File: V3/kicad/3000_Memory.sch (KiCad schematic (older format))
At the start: 4 parts, among them U3000 SST39SF040, U3001 AS6C4008-55PCN

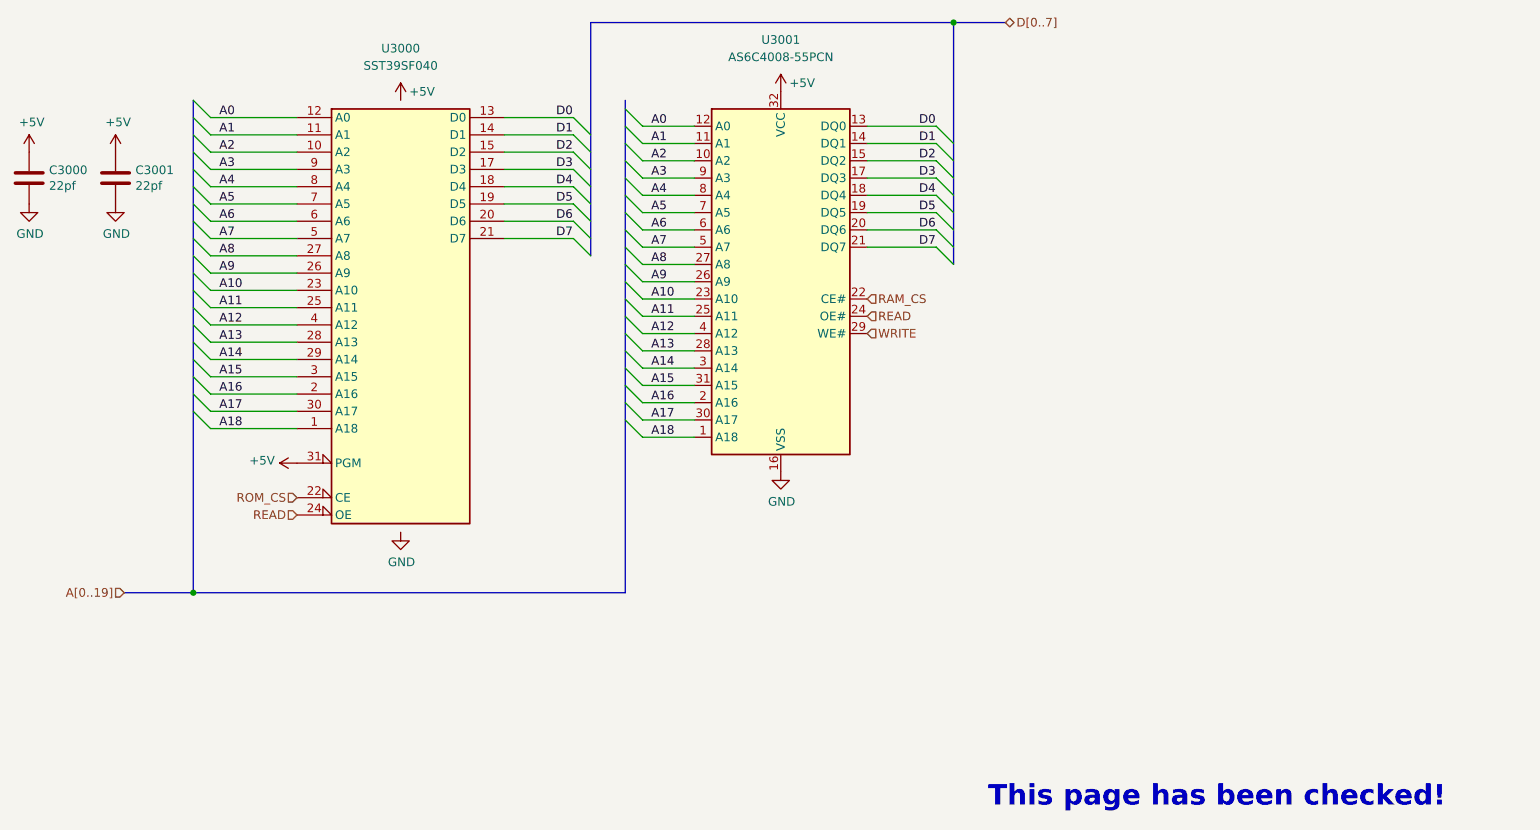
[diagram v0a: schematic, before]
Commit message: 3 1 1 m memory (#15)
* moved EEPROM files to /old

* Reworking 3.0 board

* changed footprint on RAM chip

* cleared out old memory traces

* started on rerouting

* on to autoroute

* little more cleanup

* more cleanup

* ill let the autoroute do the rest

* reroute complete

* made PQFP leads fatter

* Updated GAL logic

* Design Rule Check

* Minor pcb touch up

* gerber files

* just totally redid the whole thing

* More rearranging

* added a few caps

* Routed ROM and RAM together

* more routing

* more routes

* A lot of disorganized changes

* 3.1 CSIO SPI Bus (#9)

* Updated SPI to use CPU signals

8 bit register chip controls CS lines

* Renamed and added caps to SD page

* Cleanup

* 3.1 Resistor Replacement (#10)

* First two R arrays

* Added one more r array

* added cap for SPI FF

* Extended cpu pads (#12)

* 3.1 fix sheet hierarchy (#13)

* Fixed Schematic Heirarchy issue

* some footprints re-added to board

* Add footprints added

* Minor changes

* 3.1 redraw cpu courtyard (#14)

* moved all crtyd lines to same place in file

* Duplicate lines were causing issues

* Added pin header for SPI lines

* routed last of non-bus lines

* attempted to route memory lines

* Added new symbol and footprint

* CTS0 no longer drives an LED

* Final cleanup before memory routing

* got CTS0 and RTS mixed up

* Removed extra led from board

* Updated signature

* small changes
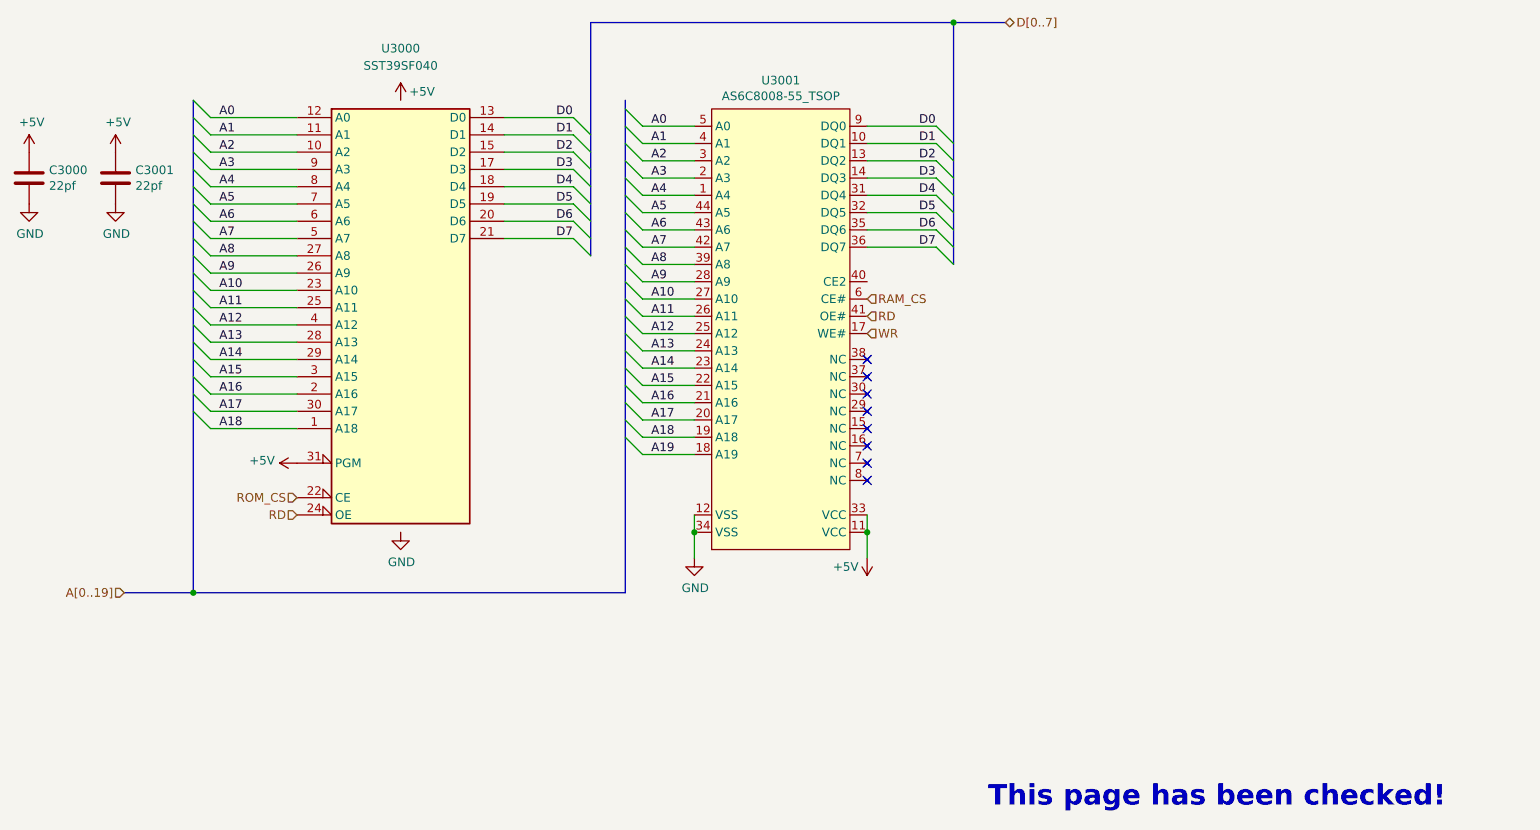
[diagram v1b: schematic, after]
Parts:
- removed U3001: AS6C4008-55PCN, Package_SO:TSOP-II-32_21.0x10.2mm_P1.27mm, symbol Memory_RAM:AS6C4008-55PCN
- added U3001: AS6C8008-55_TSOP, Package_SO:TSOP-II-44_10.16x18.41mm_P0.8mm, symbol as6c8008-55_tsop:AS6C8008-55_TSOP
- C3000, C3001: footprint Capacitor_THT:C_Rect_L4.0mm_W2.5mm_P2.50mm -> Capacitor_SMD:C_1206_3216Metric
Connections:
- net +5V: now also U3001.11 (VCC), U3001.33 (VCC)
- net A0: now also U3001.5 (A0)
- net A1: now also U3001.4 (A1)
- net A10: now also U3001.27 (A10)
- net A11: now also U3001.26 (A11)
- net A12: now also U3001.25 (A12)
- net A13: now also U3001.24 (A13)
- net A14: now also U3001.23 (A14)
- net A15: now also U3001.22 (A15)
- net A16: now also U3001.21 (A16)
- net A17: now also U3001.20 (A17)
- net A18: now also U3001.19 (A18)
- net A2: now also U3001.3 (A2)
- net A3: now also U3001.2 (A3)
- net A4: now also U3001.1 (A4)
- net A5: now also U3001.44 (A5)
- net A6: now also U3001.43 (A6)
- net A7: now also U3001.42 (A7)
- net A8: now also U3001.39 (A8)
- net A9: now also U3001.28 (A9)
- net D0: now also U3001.9 (DQ0)
- net D1: now also U3001.10 (DQ1)
- net D2: now also U3001.13 (DQ2)
- net D3: now also U3001.14 (DQ3)
- net D4: now also U3001.31 (DQ4)
- net D5: now also U3001.32 (DQ5)
- net D6: now also U3001.35 (DQ6)
- net D7: now also U3001.36 (DQ7)
- net GND: now also U3001.12 (VSS), U3001.34 (VSS)
- net RAM_CS: now also U3001.6 (CE#)
- net READ renamed RD
- net RD: now also U3001.41 (OE#)
- new net A19: U3001.18 (A19)
- new net WR: U3001.17 (WE#)
- no-connect marks 0 -> 8
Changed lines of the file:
@@
 $Descr A4 11693 8268
 encoding utf-8
-Sheet 2 9
+Sheet 2 6
 Title ""
 Date ""
@@
 Text Label 5300 3650 0    50   ~ 0
 D7
-Wire Bus Line
-	5500 2400 7600 2400
-Wire Bus Line
-	7600 2400 7900 2400
 Text HLabel 2800 5700 0    50   Input ~ 0
 A[0..19]
@@
 F 0 "C3000" H 2365 3346 50  0000 L CNN
 F 1 "22pf" H 2365 3255 50  0000 L CNN
-F 2 "Capacitor_THT:C_Rect_L4.0mm_W2.5mm_P2.50mm" H 2288 3150 50  0001 C CNN
+F 2 "Capacitor_SMD:C_1206_3216Metric" H 2288 3150 50  0001 C CNN
 F 3 "~" H 2250 3300 50  0001 C CNN
 	1    2250 3300
@@
 F 0 "C3001" H 2865 3346 50  0000 L CNN
 F 1 "22pf" H 2865 3255 50  0000 L CNN
-F 2 "Capacitor_THT:C_Rect_L4.0mm_W2.5mm_P2.50mm" H 2788 3150 50  0001 C CNN
+F 2 "Capacitor_SMD:C_1206_3216Metric" H 2788 3150 50  0001 C CNN
 F 3 "~" H 2750 3300 50  0001 C CNN
 	1    2750 3300
@@
 L power:+5V #PWR0180
 U 1 1 61F46407
-P 6600 2800
-F 0 "#PWR0180" H 6600 2650 50  0001 C CNN
-F 1 "+5V" H 6650 2850 50  0000 L CNN
-F 2 "" H 6600 2800 50  0001 C CNN
-F 3 "" H 6600 2800 50  0001 C CNN
-	1    6600 2800
-	1    0    0    -1
-$EndComp
-Text HLabel 7100 4200 2    50   Input ~ 0
-WRITE
+P 7100 5500
+F 0 "#PWR0180" H 7100 5350 50  0001 C CNN
+F 1 "+5V" H 7150 5550 50  0000 L CNN
+F 2 "" H 7100 5500 50  0001 C CNN
+F 3 "" H 7100 5500 50  0001 C CNN
+	1    7100 5500
+	-1   0    0    1
+$EndComp
 $Comp
 L power:GND #PWR0181
 U 1 1 61F61A4C
-P 6600 5000
-F 0 "#PWR0181" H 6600 4750 50  0001 C CNN
-F 1 "GND" H 6605 4827 50  0000 C CNN
-F 2 "" H 6600 5000 50  0001 C CNN
-F 3 "" H 6600 5000 50  0001 C CNN
-	1    6600 5000
+P 6100 5500
+F 0 "#PWR0181" H 6100 5250 50  0001 C CNN
+F 1 "GND" H 6105 5327 50  0000 C CNN
+F 2 "" H 6100 5500 50  0001 C CNN
+F 3 "" H 6100 5500 50  0001 C CNN
+	1    6100 5500
 	1    0    0    -1
 $EndComp
@@
 	1    0    0    -1
 $EndComp
-$Comp
-L Memory_RAM:AS6C4008-55PCN U3001
-U 1 1 62109604
-P 6600 3900
-F 0 "U3001" H 6600 5300 50  0000 C CNN
-F 1 "AS6C4008-55PCN" H 6600 5200 50  0000 C CNN
-F 2 "Package_SO:TSOP-II-32_21.0x10.2mm_P1.27mm" H 6600 4000 50  0001 C CNN
-F 3 "https://www.digikey.com/en/products/detail/alliance-memory-inc/AS6C4008-55ZIN/4234590" H 6600 4000 50  0001 C CNN
-	1    6600 3900
-	1    0    0    -1
-$EndComp
 Text HLabel 7100 4000 2    50   Input ~ 0
 RAM_CS
-Text HLabel 7100 4100 2    50   Input ~ 0
-READ
 Text HLabel 3800 5150 0    50   Input ~ 0
 ROM_CS
-Text HLabel 3800 5250 0    50   Input ~ 0
-READ
-Connection ~ 7600 2400
-$Comp
-L Memory_Flash:SST39SF040 U3000
-U 1 1 625638C2
-P 4400 4150
-F 0 "U3000" H 4400 5750 50  0000 C CNN
-F 1 "SST39SF040" H 4400 5650 50  0000 C CNN
-F 2 "Package_DIP:DIP-32_W15.24mm_LongPads" H 4400 4450 50  0001 C CNN
-F 3 "http://ww1.microchip.com/downloads/en/DeviceDoc/25022B.pdf" H 4400 4450 50  0001 C CNN
-	1    4400 4150
-	1    0    0    -1
-$EndComp
 Entry Wire Line
 	3200 2850 3300 2950
@@
 Wire Bus Line
 	3200 5700 5700 5700
+Text HLabel 7100 4100 2    50   Input ~ 0
+RD
+Text HLabel 7100 4200 2    50   Input ~ 0
+WR
+Text HLabel 3800 5250 0    50   Input ~ 0
+RD
+$Comp
+L Memory_Flash:SST39SF040 U3000
+U 1 1 625638C2
+P 4400 4150
+F 0 "U3000" H 4400 5750 50  0000 C CNN
+F 1 "SST39SF040" H 4400 5650 50  0000 C CNN
+F 2 "Package_DIP:DIP-32_W15.24mm_LongPads" H 4400 4450 50  0001 C CNN
+F 3 "http://ww1.microchip.com/downloads/en/DeviceDoc/25022B.pdf" H 4400 4450 50  0001 C CNN
+	1    4400 4150
+	1    0    0    -1
+$EndComp
+$Comp
+L as6c8008-55_tsop:AS6C8008-55_TSOP U3001
+U 1 1 63A1386B
+P 6600 3900
+F 0 "U3001" H 6600 5065 50  0000 C CNN
+F 1 "AS6C8008-55_TSOP" H 6600 4974 50  0000 C CNN
+F 2 "Package_SO:TSOP-II-44_10.16x18.41mm_P0.8mm" H 6600 4973 50  0001 C CNN
+F 3 "https://www.alliancememory.com/wp-content/uploads/pdf/AS6C4008.pdf" H 6600 4000 50  0001 C CNN
+	1    6600 3900
+	1    0    0    -1
+$EndComp
+Entry Wire Line
+	5700 4800 5800 4900
+Wire Wire Line
+	5800 4900 6100 4900
+Text Label 5850 4900 0    50   ~ 0
+A19
+Wire Bus Line
+	5500 2400 7600 2400
+Connection ~ 7600 2400
+Wire Bus Line
+	7600 2400 7900 2400
+Wire Wire Line
+	7100 5250 7100 5350
+Connection ~ 7100 5350
+Wire Wire Line
+	7100 5350 7100 5500
+Wire Wire Line
+	6100 5250 6100 5350
+Connection ~ 6100 5350
+Wire Wire Line
+	6100 5350 6100 5500
+NoConn ~ 7100 4350
+NoConn ~ 7100 4450
+NoConn ~ 7100 4550
+NoConn ~ 7100 4650
+NoConn ~ 7100 4750
+NoConn ~ 7100 4850
+NoConn ~ 7100 4950
+NoConn ~ 7100 5050
 Wire Bus Line
 	5500 2400 5500 3750
